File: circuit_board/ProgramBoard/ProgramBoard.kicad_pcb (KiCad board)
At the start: 2 copper layers, 55.9 x 39.4 mm, 12 parts, among them J1 BARREL_JACK, P1 IDC-10, P2 HEADER_6, P3 HEADER_3, P4 HEADER_3, P5 HEADER_3, U1 SparkFun_FT231X_Breakout

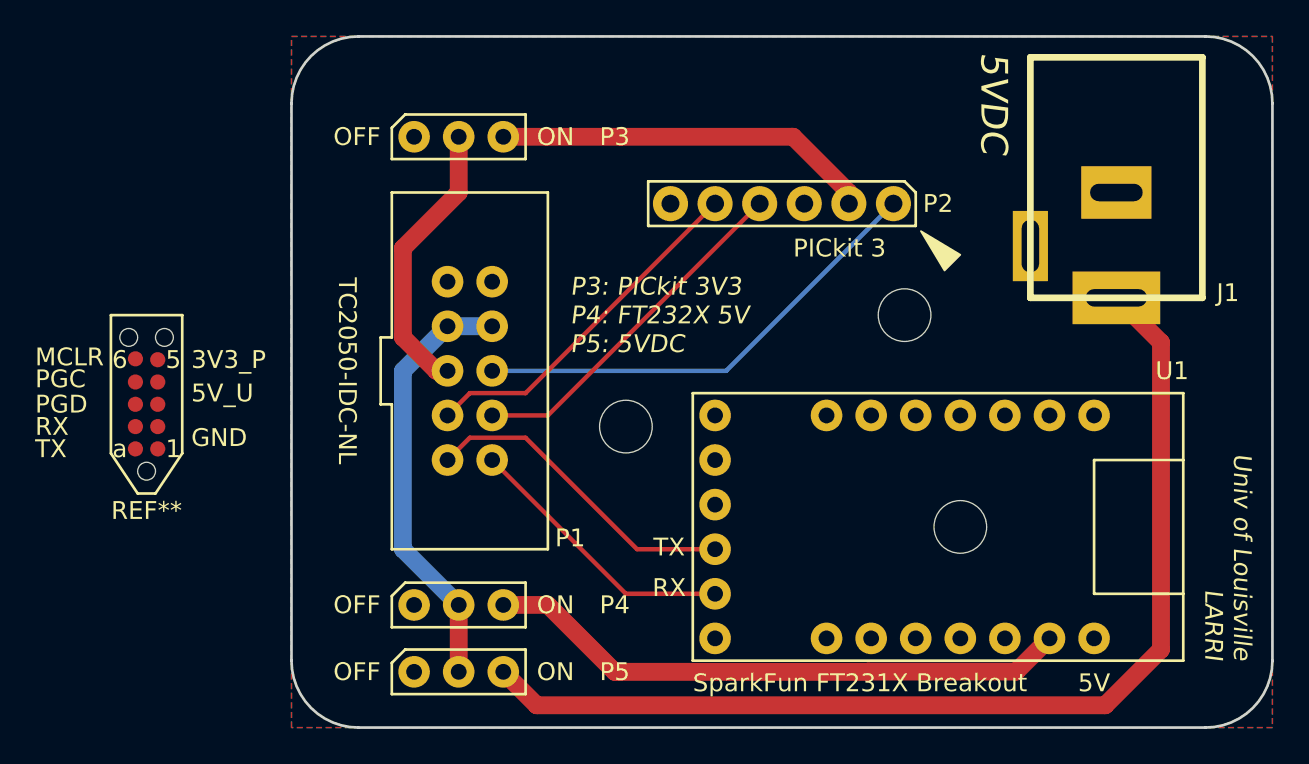
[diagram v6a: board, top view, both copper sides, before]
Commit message: testing pins added
updated PCB design:
added testing pins on the SensorDemo.
ProgramBoard modified GND connections.
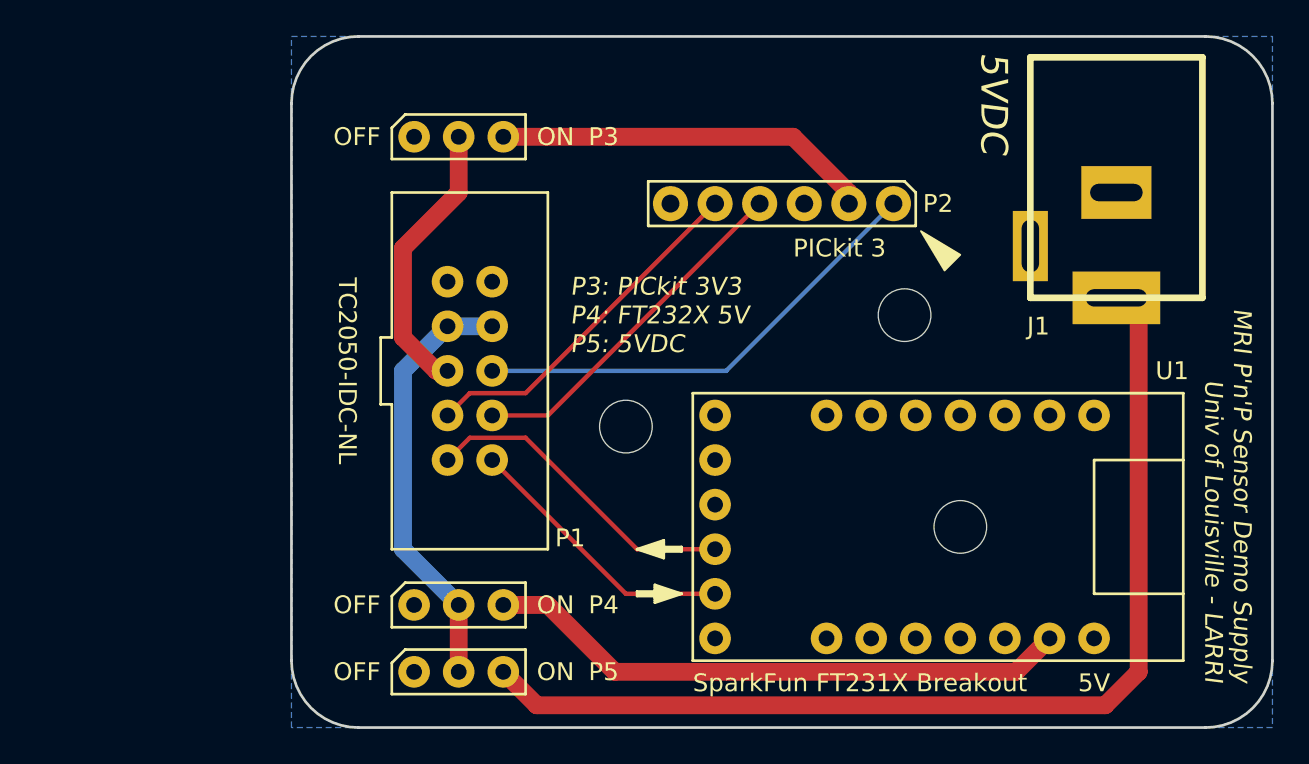
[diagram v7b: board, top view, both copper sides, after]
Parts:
- removed REF**: TC2050, SensorDemo_pcb:TC2050
- moved G*** 32.6 mm to (108.8, 91.2)
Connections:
- J1 pad 2: Net-(J1-Pad2) -> GND
- J1 pad 3: GND -> (no net)
- P2 pad 6: Net-(P2-Pad6) -> (no net)
- P3 pad 1: Net-(P3-Pad1) -> (no net)
- P4 pad 1: Net-(P4-Pad1) -> (no net)
- P5 pad 1: Net-(P5-Pad1) -> (no net)
- U1 pad 1: Net-(U1-Pad1) -> (no net)
- U1 pad 10: Net-(U1-Pad10) -> (no net)
- U1 pad 13: Net-(U1-Pad13) -> (no net)
- U1 pad 14: Net-(U1-Pad14) -> (no net)
- U1 pad 15: Net-(U1-Pad15) -> (no net)
- U1 pad 16: Net-(U1-Pad16) -> (no net)
- U1 pad 17: Net-(U1-Pad17) -> (no net)
- U1 pad 18: Net-(U1-Pad18) -> (no net)
- U1 pad 2: Net-(U1-Pad2) -> (no net)
- U1 pad 20: Net-(U1-Pad20) -> GND
- U1 pad 3: Net-(U1-Pad3) -> (no net)
- U1 pad 4: Net-(U1-Pad4) -> (no net)
- U1 pad 5: Net-(U1-Pad5) -> (no net)
- U1 pad 6: Net-(U1-Pad6) -> (no net)
- U1 pad 7: Net-(U1-Pad7) -> (no net)
- U1 pad 8: Net-(U1-Pad8) -> GND
- U1 pad 9: Net-(U1-Pad9) -> (no net)
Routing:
- net Net-(J1-Pad1): track 60.7 -> 59.6 mm
- removed copper zone on F.Cu, net GND
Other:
- board text added: "Daniel &"
- board text added: "MRI P'n'P Sensor Demo Supply Univ of Louisville - LARRI"
- board text removed: "3V3_P"
- board text removed: "5V_U"
- board text removed: "GND"
- board text removed: "MCLR"
- board text removed: "PGC"
- board text removed: "PGD"
- board text removed: "RX"
- board text removed: "TX"
- board text removed: "Univ of Louisville LARRI"

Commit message: modified according to Doug
on SensorDemo, fiducial marks are added, via size changed to .25mm and .55mm, decreased solder mask gap between pins on MSOP8 package.
the minimum JLC can take between pins is .2mm for green mask.
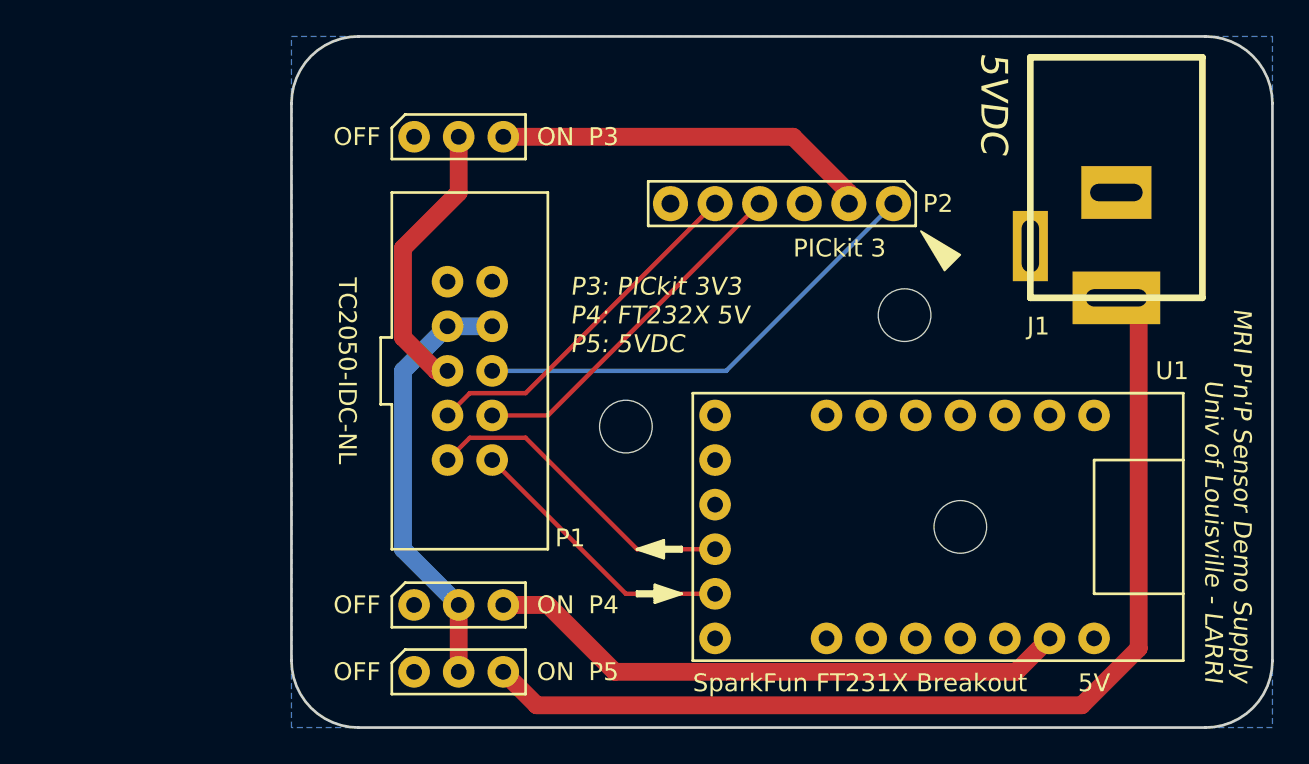
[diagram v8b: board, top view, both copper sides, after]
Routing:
- net Net-(J1-Pad1): track 59.6 -> 58.8 mm
